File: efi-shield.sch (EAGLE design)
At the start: 67 parts, among them J1 PWMH, J2 PWMI, J3 COMM, J4 PWR, J5 ADCL, J6 ADCH, J7 AMPSEAL-23POS-HEADER, J8 SPI, Q1 PN2222, Q2 FJPF13009, U1 TXS0104E, U2 TXS0104E, U3 MCP3304, U4 MCP6024, U5 MCP6024

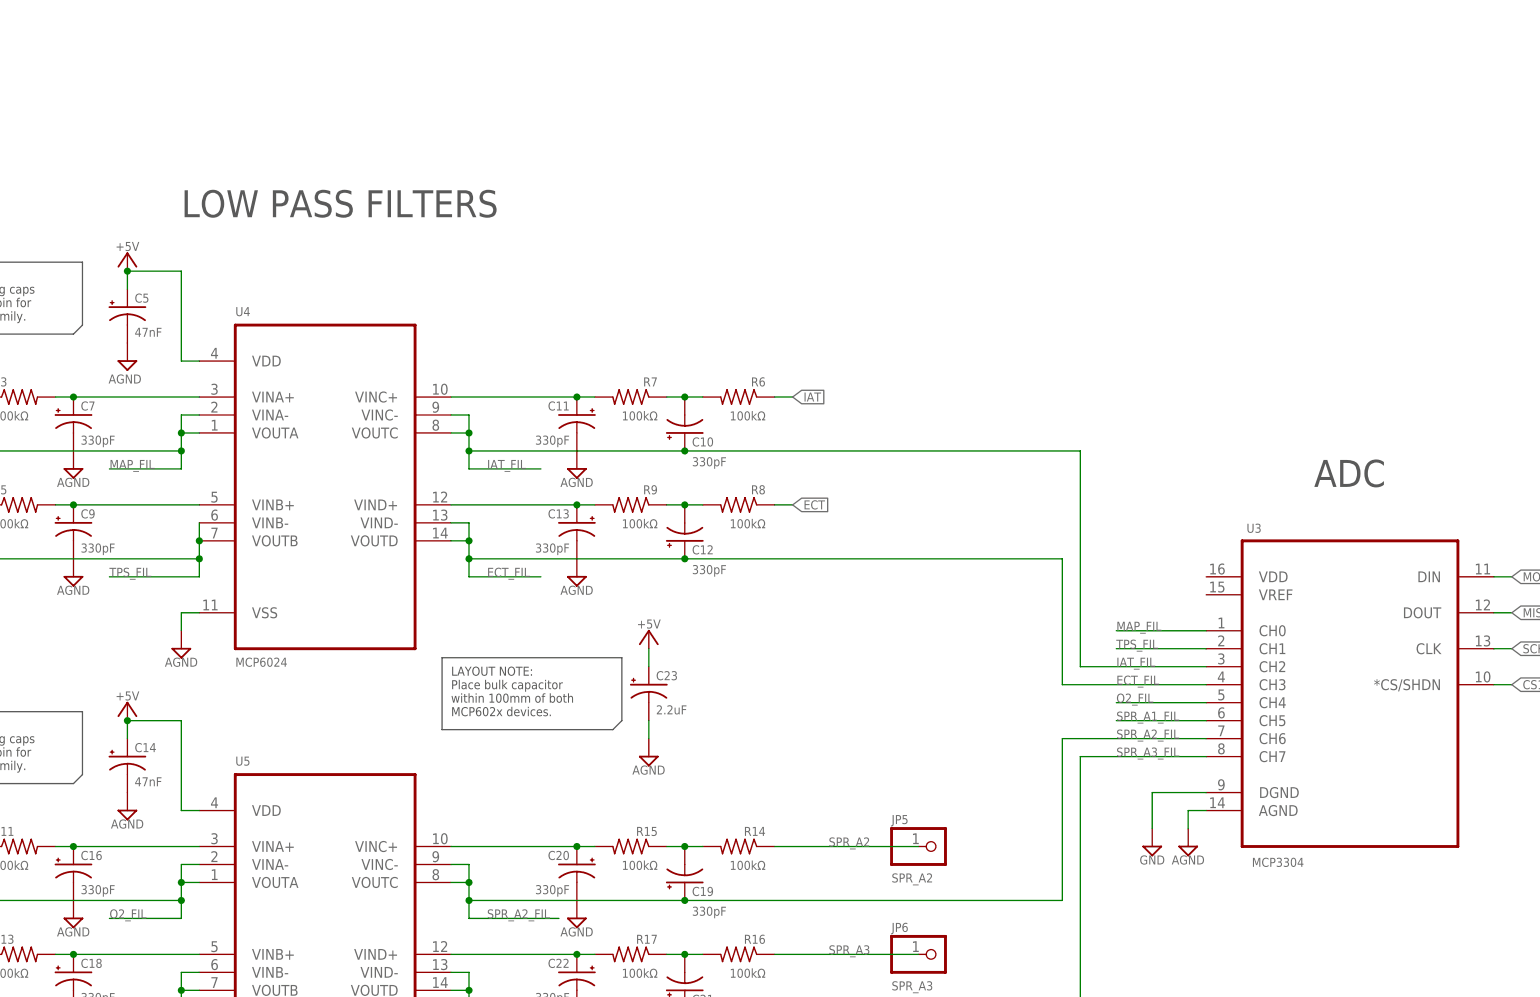
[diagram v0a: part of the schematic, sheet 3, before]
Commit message: Cleaned up grounding and MCP3304 ADC layout.
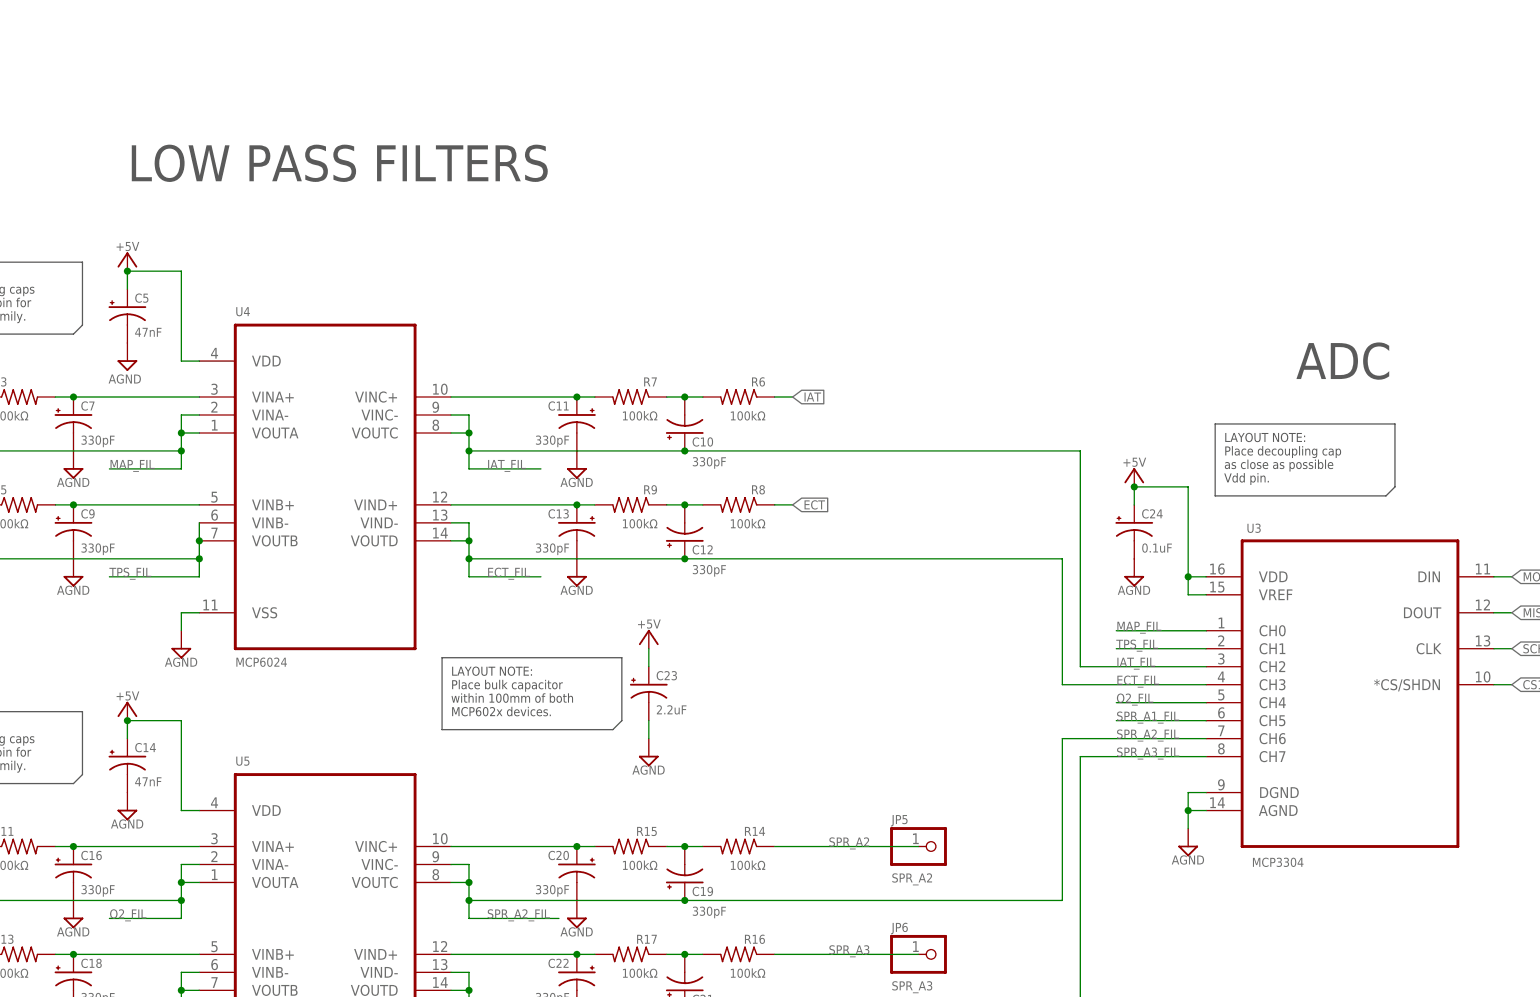
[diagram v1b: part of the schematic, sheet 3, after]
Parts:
- added C24: 0.1uF, cpsmv:CAP-JKE
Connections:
- net N$23 renamed SPR_IN1
- net N$24 renamed SPR_IN2
- net N$25 renamed SPR_IN3
- net +5V: now also C24.1, U3.VDD, U3.VREF
- net AGND: now also C24.2, U3.DGND
- net GND: no longer U3.DGND
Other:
- note added: "LAYOUT NOTE: Place decoupling cap as close as possible Vdd pin."
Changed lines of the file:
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@@
 <part name="SUPPLY20" library="supply2" deviceset="AGND" device=""/>
 <part name="SUPPLY21" library="supply2" deviceset="AGND" device=""/>
-<part name="SUPPLY22" library="supply2" deviceset="GND" device=""/>
 <part name="U$1" library="cpsmv" deviceset="CPSMV-FRAME" device=""/>
 <part name="U$2" library="cpsmv" deviceset="CPSMV-FRAME" device=""/>
@@
 <part name="U$5" library="cpsmv" deviceset="CPSMV-FRAME" device=""/>
 <part name="U$6" library="cpsmv" deviceset="CPSMV-FRAME" device=""/>
+<part name="C24" library="cpsmv" deviceset="CAP-JKE" device="" value="0.1uF"/>
+<part name="SUPPLY22" library="supply2" deviceset="AGND" device=""/>
+<part name="P+10" library="supply1" deviceset="+5V" device=""/>
 </parts>
 <sheets>
@@
 CANRX
 CANTX</text>
-<text x="139.7" y="190.5" size="3.81" layer="97">ARDUINO DUE</text>
-<text x="58.42" y="190.5" size="3.81" layer="97">AMPSEAL </text>
+<text x="139.7" y="193.04" size="5.08" layer="97">ARDUINO DUE</text>
+<text x="43.18" y="193.04" size="5.08" layer="97">AMPSEAL </text>
 <text x="223.52" y="157.48" size="1.27" layer="97" align="center-left">RESET</text>
-<text x="284.48" y="190.5" size="3.81" layer="97">SPI</text>
-<text x="55.88" y="101.6" size="3.81" layer="97">SPARE INPUTS</text>
+<text x="284.48" y="193.04" size="5.08" layer="97">SPI</text>
+<text x="45.72" y="101.6" size="5.08" layer="97">SPARE INPUTS</text>
 <text x="336.55" y="15.24" size="2.54" layer="94" font="vector">Alex Pink</text>
 <text x="361.95" y="5.08" size="2.54" layer="94" font="vector">01</text>
@@
 <label x="43.18" y="129.54" size="1.27" layer="95" font="vector" rot="R180"/>
 </segment>
+<segment>
+<pinref part="JP1" gate="G$1" pin="1"/>
+<wire x1="71.12" y1="91.44" x2="55.88" y2="91.44" width="0.1524" layer="91"/>
+<label x="55.88" y="91.44" size="1.27" layer="95"/>
+</segment>
 </net>
 <net name="SPR_IN2" class="0">
@@
 <label x="43.18" y="127" size="1.27" layer="95" font="vector" rot="R180"/>
 </segment>
+<segment>
+<pinref part="JP2" gate="G$1" pin="1"/>
+<wire x1="71.12" y1="81.28" x2="55.88" y2="81.28" width="0.1524" layer="91"/>
+<label x="55.88" y="81.28" size="1.27" layer="95"/>
+</segment>
 </net>
 <net name="SPR_IN3" class="0">
@@
 <label x="43.18" y="124.46" size="1.27" layer="95" font="vector" rot="R180"/>
 </segment>
-</net>
-<net name="N$23" class="0">
-<segment>
-<pinref part="JP1" gate="G$1" pin="1"/>
-<wire x1="71.12" y1="91.44" x2="63.5" y2="91.44" width="0.1524" layer="91"/>
-</segment>
-</net>
-<net name="N$24" class="0">
-<segment>
-<pinref part="JP2" gate="G$1" pin="1"/>
-<wire x1="71.12" y1="81.28" x2="63.5" y2="81.28" width="0.1524" layer="91"/>
-</segment>
-</net>
-<net name="N$25" class="0">
 <segment>
 <pinref part="JP3" gate="G$1" pin="1"/>
-<wire x1="71.12" y1="71.12" x2="63.5" y2="71.12" width="0.1524" layer="91"/>
+<wire x1="71.12" y1="71.12" x2="55.88" y2="71.12" width="0.1524" layer="91"/>
+<label x="55.88" y="71.12" size="1.27" layer="95"/>
 </segment>
 </net>
@@
 <description>ACTUATORS</description>
 <plain>
-<text x="264.16" y="153.67" size="3.81" layer="97">SPARK</text>
-<text x="147.32" y="153.67" size="3.81" layer="97">FUEL</text>
+<text x="264.16" y="151.13" size="5.08" layer="97">SPARK</text>
+<text x="147.32" y="151.13" size="5.08" layer="97">FUEL</text>
 <text x="336.55" y="15.24" size="2.54" layer="94" font="vector">Alex Pink</text>
 <text x="361.95" y="5.08" size="2.54" layer="94" font="vector">01</text>
@@
 <wire x1="194.31" y1="135.89" x2="194.31" y2="127" width="0.1524" layer="97"/>
 <wire x1="194.31" y1="127" x2="193.04" y2="125.73" width="0.1524" layer="97"/>
-<text x="132.08" y="198.12" size="3.81" layer="97">LOW PASS FILTERS</text>
-<text x="292.1" y="160.02" size="3.81" layer="97">ADC</text>
+<text x="124.46" y="203.2" size="5.08" layer="97">LOW PASS FILTERS</text>
+<text x="289.56" y="175.26" size="5.08" layer="97">ADC</text>
 <text x="336.55" y="15.24" size="2.54" layer="94" font="vector">Alex Pink</text>
 <text x="361.95" y="5.08" size="2.54" layer="94" font="vector">01</text>
 <text x="334.01" y="20.32" size="2.54" layer="94" font="vector">Filters &amp; ADC</text>
+<text x="279.4" y="167.64" size="1.27" layer="97" align="top-left">LAYOUT NOTE:
+Place decoupling cap
+as close as possible
+Vdd pin.</text>
+<wire x1="278.13" y1="168.91" x2="303.53" y2="168.91" width="0.1524" layer="97"/>
+<wire x1="302.26" y1="158.75" x2="278.13" y2="158.75" width="0.1524" layer="97"/>
+<wire x1="278.13" y1="158.75" x2="278.13" y2="168.91" width="0.1524" layer="97"/>
+<wire x1="303.53" y1="168.91" x2="303.53" y2="160.02" width="0.1524" layer="97"/>
+<wire x1="303.53" y1="160.02" x2="302.26" y2="158.75" width="0.1524" layer="97"/>
 </plain>
 <instances>
@@
 <instance part="SUPPLY20" gate="G$1" x="274.32" y="109.22"/>
 <instance part="SUPPLY21" gate="G$1" x="198.12" y="121.92"/>
-<instance part="SUPPLY22" gate="GND" x="269.24" y="109.22"/>
 <instance part="U$2" gate="G$1" x="0" y="0"/>
+<instance part="C24" gate="G$1" x="266.7" y="154.94"/>
+<instance part="SUPPLY22" gate="G$1" x="266.7" y="147.32"/>
+<instance part="P+10" gate="1" x="266.7" y="162.56"/>
 </instances>
 <busses>
@@
 <pinref part="C23" gate="G$1" pin="1"/>
 <wire x1="198.12" y1="137.16" x2="198.12" y2="134.62" width="0.1524" layer="91"/>
+</segment>
+<segment>
+<pinref part="U3" gate="A" pin="VREF"/>
+<wire x1="276.86" y1="144.78" x2="274.32" y2="144.78" width="0.1524" layer="91"/>
+<wire x1="274.32" y1="144.78" x2="274.32" y2="147.32" width="0.1524" layer="91"/>
+<pinref part="U3" gate="A" pin="VDD"/>
+<wire x1="274.32" y1="147.32" x2="276.86" y2="147.32" width="0.1524" layer="91"/>
+<wire x1="274.32" y1="147.32" x2="274.32" y2="160.02" width="0.1524" layer="91"/>
+<junction x="274.32" y="147.32"/>
+<wire x1="274.32" y1="160.02" x2="266.7" y2="160.02" width="0.1524" layer="91"/>
+<pinref part="C24" gate="G$1" pin="1"/>
+<wire x1="266.7" y1="160.02" x2="266.7" y2="157.48" width="0.1524" layer="91"/>
+<pinref part="P+10" gate="1" pin="+5V"/>
+<junction x="266.7" y="160.02"/>
 </segment>
 </net>
@@
 <pinref part="SUPPLY20" gate="G$1" pin="AGND"/>
 <wire x1="274.32" y1="114.3" x2="274.32" y2="111.76" width="0.1524" layer="91"/>
+<pinref part="U3" gate="A" pin="DGND"/>
+<wire x1="276.86" y1="116.84" x2="274.32" y2="116.84" width="0.1524" layer="91"/>
+<wire x1="274.32" y1="116.84" x2="274.32" y2="114.3" width="0.1524" layer="91"/>
+<junction x="274.32" y="114.3"/>
+</segment>
+<segment>
+<pinref part="C24" gate="G$1" pin="2"/>
+<pinref part="SUPPLY22" gate="G$1" pin="AGND"/>
 </segment>
 </net>
@@
 </segment>
 </net>
-<net name="GND" class="0">
-<segment>
-<pinref part="U3" gate="A" pin="DGND"/>
-<wire x1="276.86" y1="116.84" x2="269.24" y2="116.84" width="0.1524" layer="91"/>
-<wire x1="269.24" y1="116.84" x2="269.24" y2="111.76" width="0.1524" layer="91"/>
-<pinref part="SUPPLY22" gate="GND" pin="GND"/>
-</segment>
-</net>

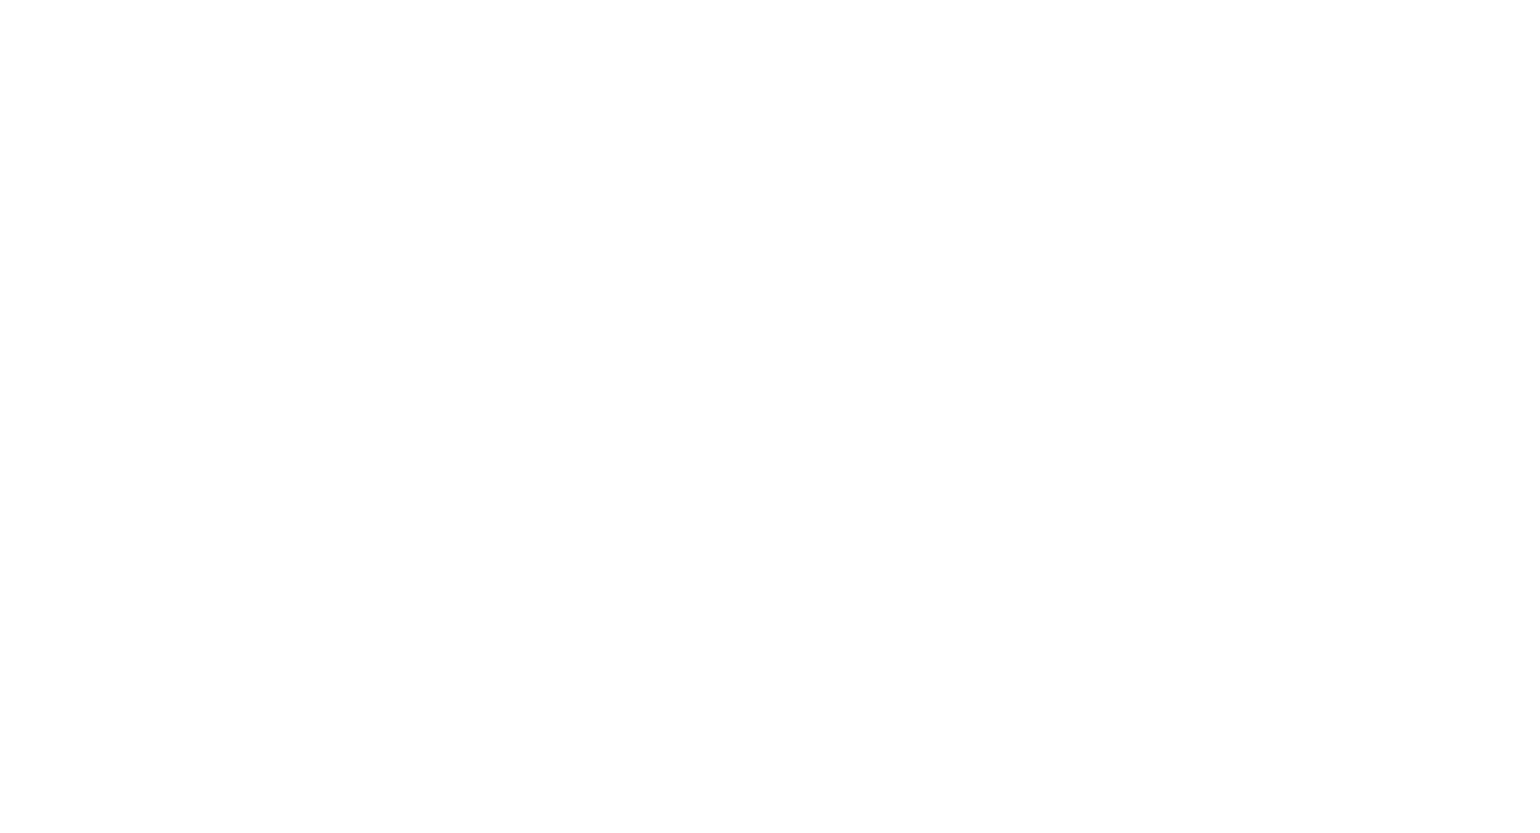
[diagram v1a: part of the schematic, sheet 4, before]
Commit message: First revision of tach circuit added.
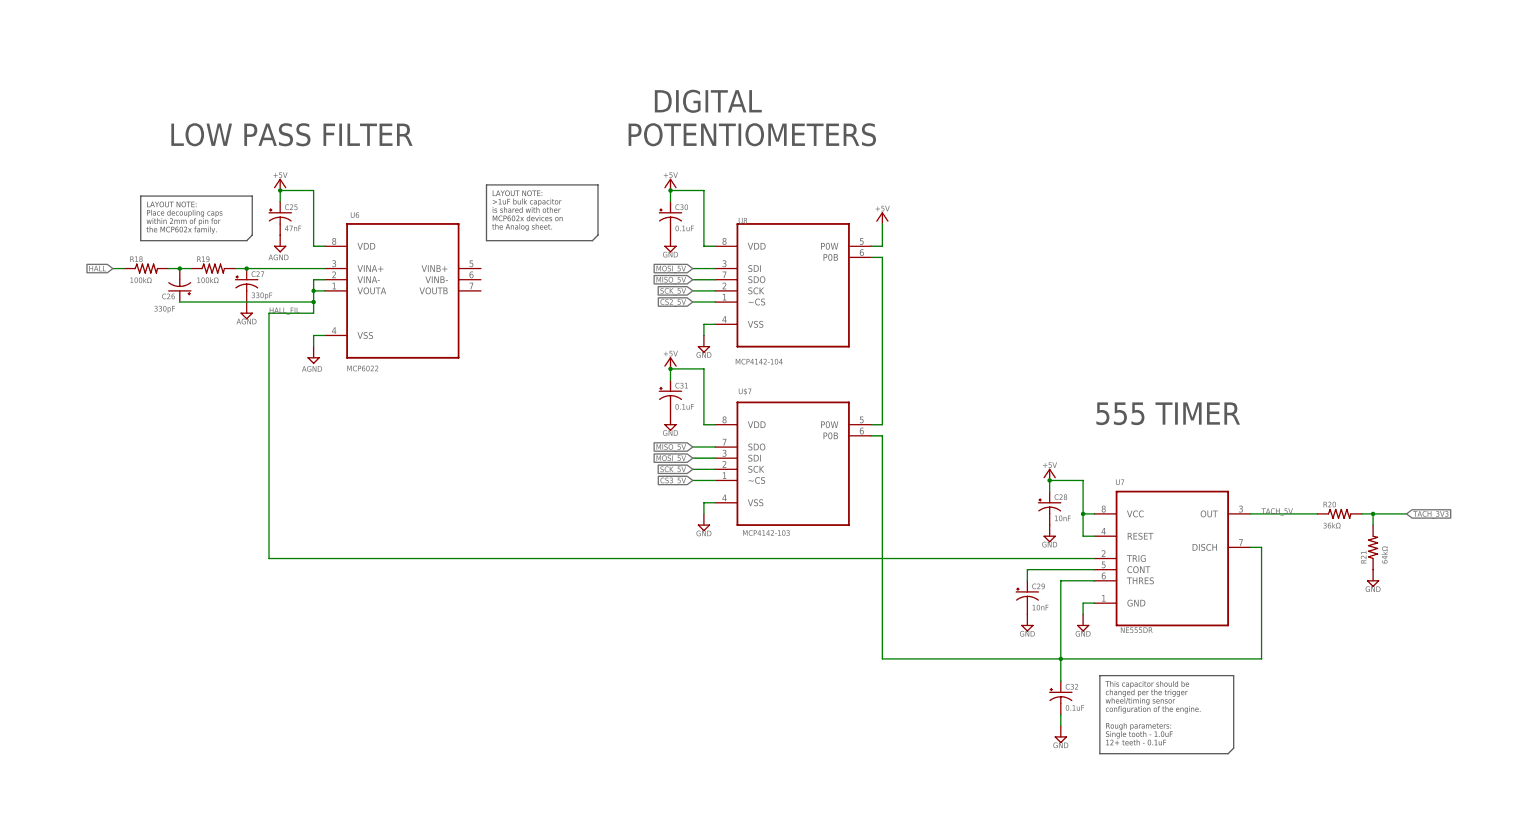
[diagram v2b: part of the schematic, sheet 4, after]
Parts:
- added C25: 47nF, cpsmv:CAP-JKE
- added C26, C27: 330pF, cpsmv:CAP-JKE
- added C28, C29: 10nF, cpsmv:CAP-JKE
- added C30, C31, C32: 0.1uF, cpsmv:CAP-JKE
- added R18, R19: 100kΩ, cpsmv:RES-JKE
- added R20: 36kΩ, cpsmv:RES-JKE
- added R21: 64kΩ, cpsmv:RES-JKE
- added U$7: MCP4142-103, cpsmv:MCP4142-103E/P
- added U6: MCP6022, cpsmv:MCP6022-I/SN
- added U7: NE555DR, cpsmv:NE555DR
- added U8: MCP4142-104, cpsmv:MCP4142-104E/P
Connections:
- removed net TACH: J2.3
- new net HALL: R18.1
- new net HALL_FIL: C26.1, U6.VINA-, U6.VOUTA, U7.TRIG
- new net N$13: C27.1, R19.2, U6.VINA+
- new net N$22: C26.2, R18.2, R19.1
- new net N$23: U$7.P0W, U8.P0B
- new net N$24: C29.1, U7.CONT
- new net N$4: C32.1, U$7.P0B, U7.DISCH, U7.THRES
- new net TACH_3V3: J2.3, R20.2, R21.2
- new net TACH_5V: R20.1, U7.OUT
- net +5V: now also C25.1, C28.1, C30.1, C31.1, U$7.VDD, U6.VDD, U7.RESET, U7.VCC, U8.P0W, U8.VDD
- net AGND: now also C25.2, C27.2, U6.VSS
- net CS2_5V: now also U8.~CS
- net CS3_5V: now also U$7.~CS
- net GND: now also C28.2, C29.2, C30.2, C31.2, C32.2, R21.1, U$7.VSS, U7.GND, U8.VSS
- net MISO_5V: now also U$7.SDO, U8.SDO
- net MOSI_5V: now also U$7.SDI, U8.SDI
- net SCK_5V: now also U$7.SCK, U8.SCK
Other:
- note added: "555 TIMER"
- note added: "Analog Inputs"
- note added: "DIGITAL POTENTIOMETERS"
- note added: "LAYOUT NOTE: >1uF bulk capacitor is shared with other MCP602x devices on the Analog sheet."
- note added: "LOW PASS FILTER"
- note added: "This capacitor should be changed per the trigger wheel/timing sensor configuration of the engine. Rough parameters: Single tooth - 1.0uF 12+ teeth - 0.1uF"
- note removed: "Filters & ADC"
